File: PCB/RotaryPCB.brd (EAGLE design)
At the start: 114.5 x 67.5 mm, 4 parts

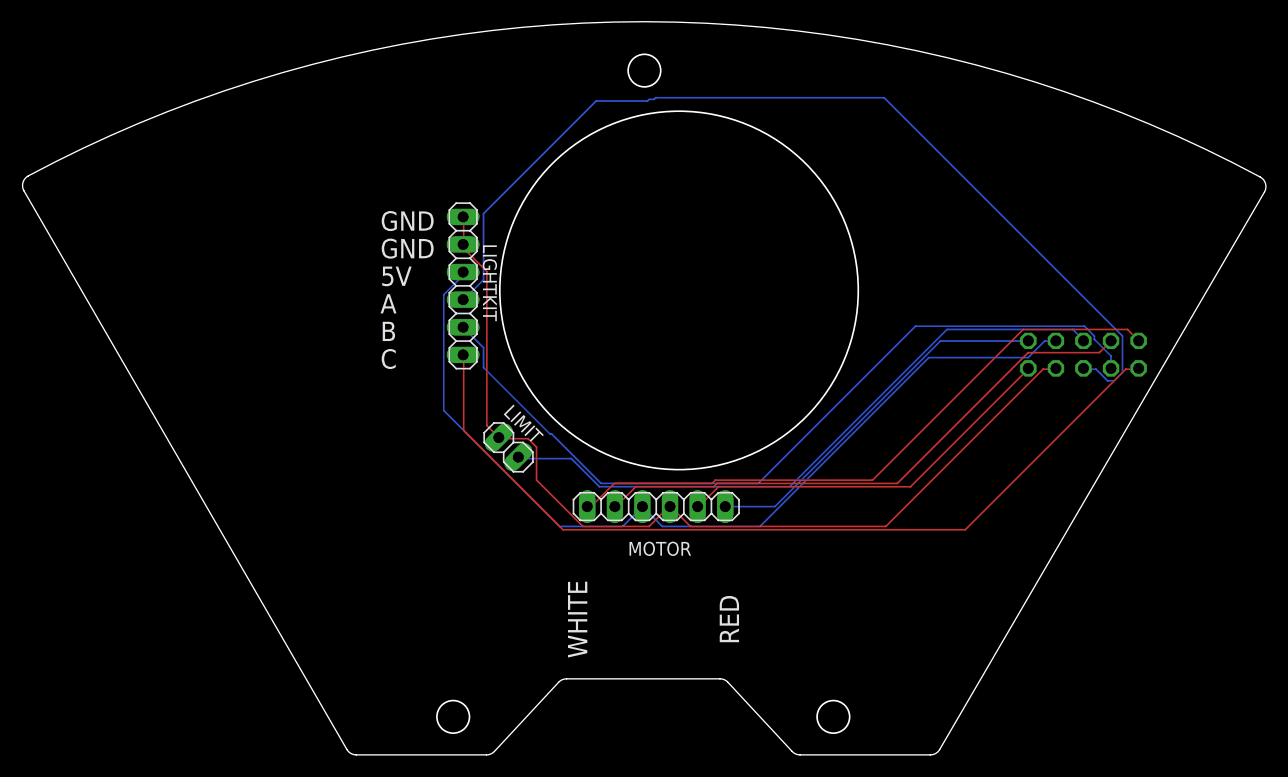
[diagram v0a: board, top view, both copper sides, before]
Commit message: Latest version of Eagle board files plus Eagle v9 version
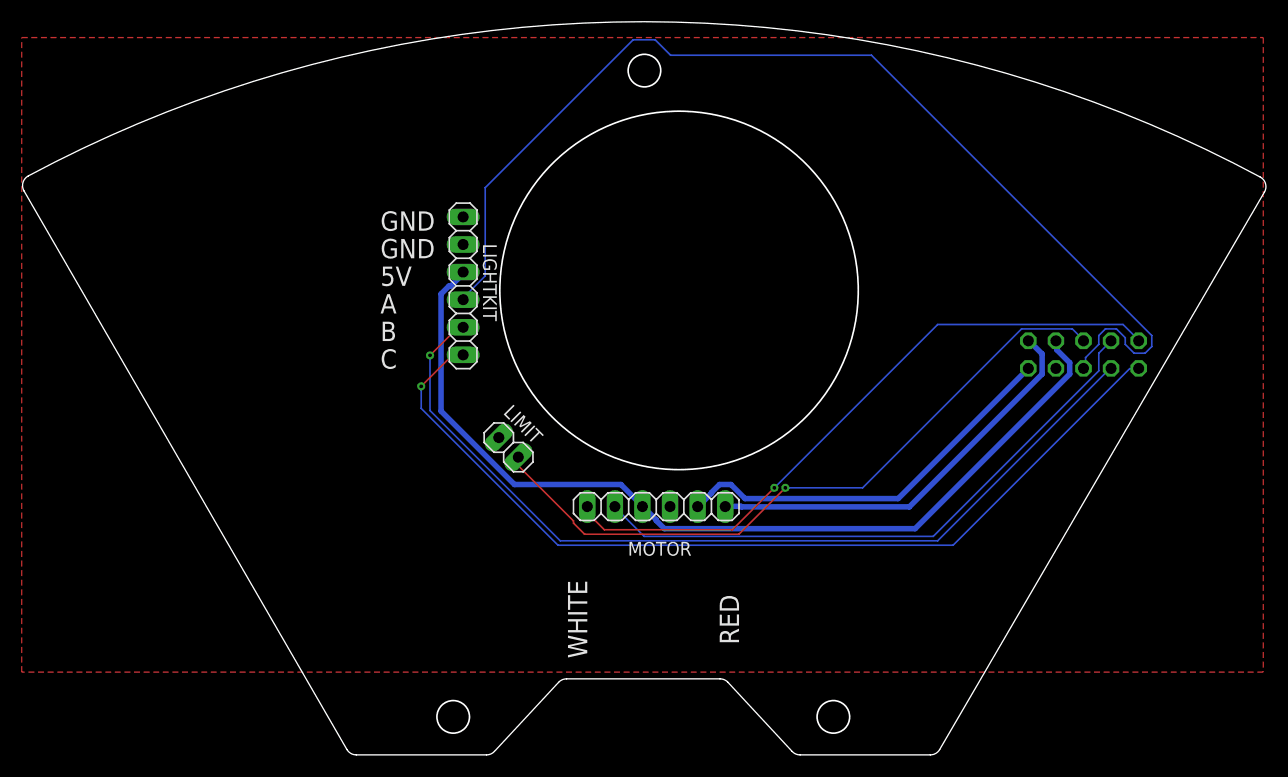
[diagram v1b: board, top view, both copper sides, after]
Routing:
- net GND: track 85.7 -> 0.00 mm
- net LKIT_A: track 88.8 -> 100.7 mm
- net LKIT_B: track 75.1 -> 83.5 mm, vias 0 -> 1
- net LKIT_C: track 79.0 -> 85.1 mm, vias 0 -> 1
- net RTR_LIMIT: track 59.7 -> 63.9 mm, vias 0 -> 1
- net RMOT2: track 34.2 -> 37.9 mm
- net RTR_ENA: track 52.0 -> 55.3 mm
- net +5V: track 82.8 -> 85.6 mm
- net RTR_ENB: track 58.0 -> 60.5 mm, vias 0 -> 1
- net RMOT1: track 35.7 -> 36.8 mm
- added copper zone on layer 1, net GND

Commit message: This version uses thicker traces and adds a copper pour. The lifter board is a four layer board. The order of the connection pins on the rotary has changed. Do NOT use the same cable as the older board. The order was changed to allow using a silicone ribbon cable.
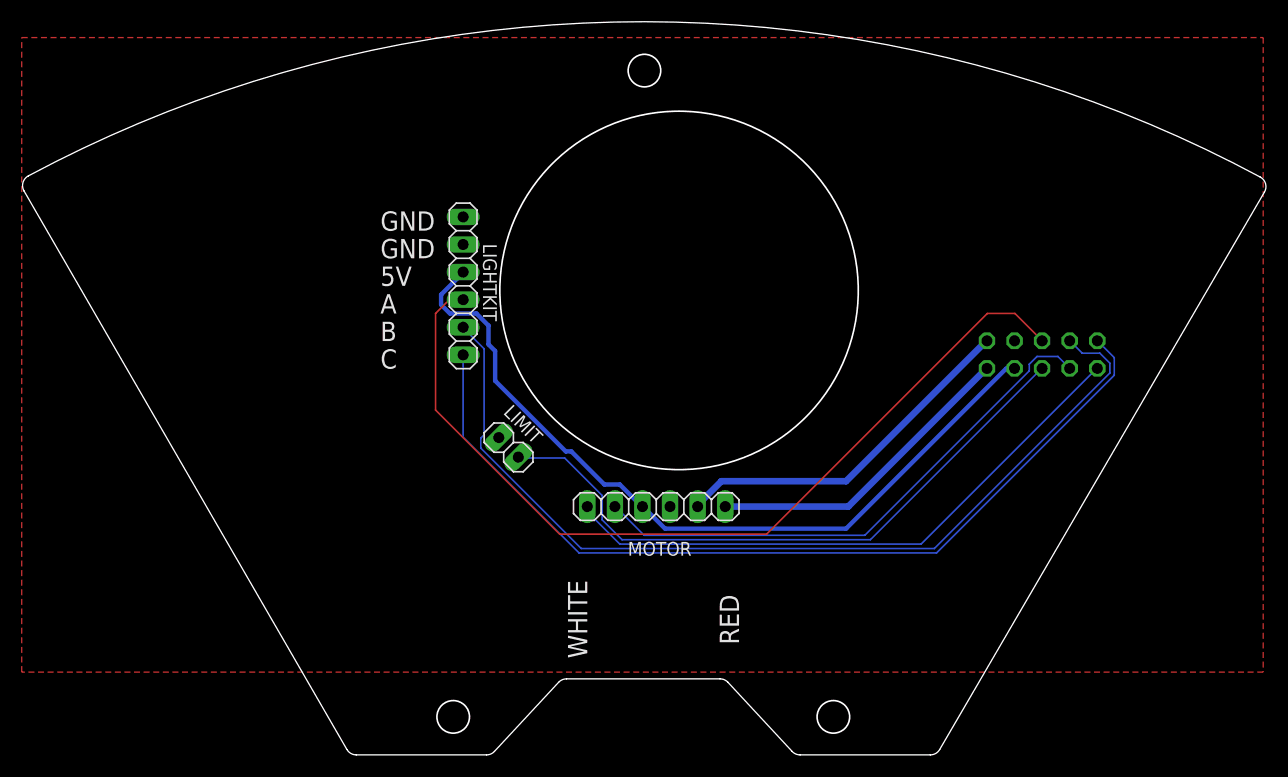
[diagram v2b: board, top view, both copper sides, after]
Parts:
- moved INPUT 3.81 mm to (93.9, 41.9)
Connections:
- net +5V: now also INPUT.7; no longer INPUT.8
- net GND: now also INPUT.8; no longer INPUT.7
- net LKIT_A: now also INPUT.6; no longer INPUT.5
- net LKIT_B: now also INPUT.4; no longer INPUT.3
- net LKIT_C: now also INPUT.2; no longer INPUT.1
- net RMOT1: now also INPUT.10; no longer INPUT.9
- net RMOT2: now also INPUT.9; no longer INPUT.10
- net RTR_ENA: now also INPUT.3; no longer INPUT.4
- net RTR_ENB: now also INPUT.1; no longer INPUT.2
- net RTR_LIMIT: now also INPUT.5; no longer INPUT.6
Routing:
- net LKIT_A: track 100.7 -> 82.0 mm
- net +5V: track 85.6 -> 73.9 mm
- net RMOT2: track 37.9 -> 29.4 mm
- net RTR_ENB: track 60.5 -> 55.4 mm, vias 1 -> 0
- net RTR_ENA: track 55.3 -> 50.6 mm
- net RTR_LIMIT: track 63.9 -> 59.3 mm, vias 1 -> 0
- net RMOT1: track 36.8 -> 33.1 mm
- net LKIT_C: track 85.1 -> 82.5 mm, vias 1 -> 0
- net LKIT_B: track 83.5 -> 85.9 mm, vias 1 -> 0
